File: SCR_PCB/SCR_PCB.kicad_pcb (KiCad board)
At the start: 2 copper layers, 97.4 x 87 mm, 96 parts, among them J2 Conn_01x03, Q1 QM6006D, Q2 QM6006D, Q3 QM6006D, Q4 QM6006D, U2 NA555D, U3 NA555D, U4 SFH617A-1, U5 SFH617A-1, U6 SFH617A-1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

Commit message: Coplete SCR PCB
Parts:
- added G***: LOGO, LOGO, F.Cu at (1.40, -12.0)
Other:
- board text added: "J.Soszyński 17.05.26"
- board text added: "SCR Full Bridge COntroll PCB"

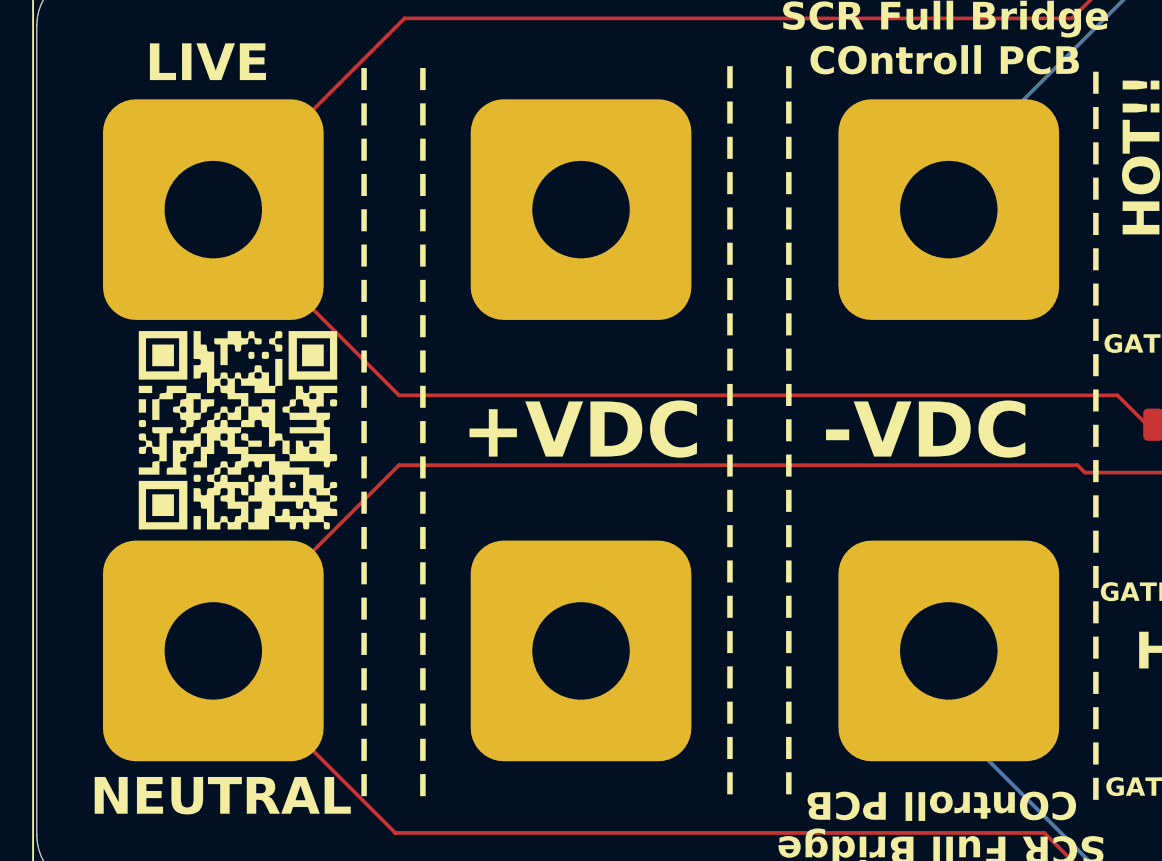
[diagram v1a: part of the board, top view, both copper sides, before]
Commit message: start Controller schematic
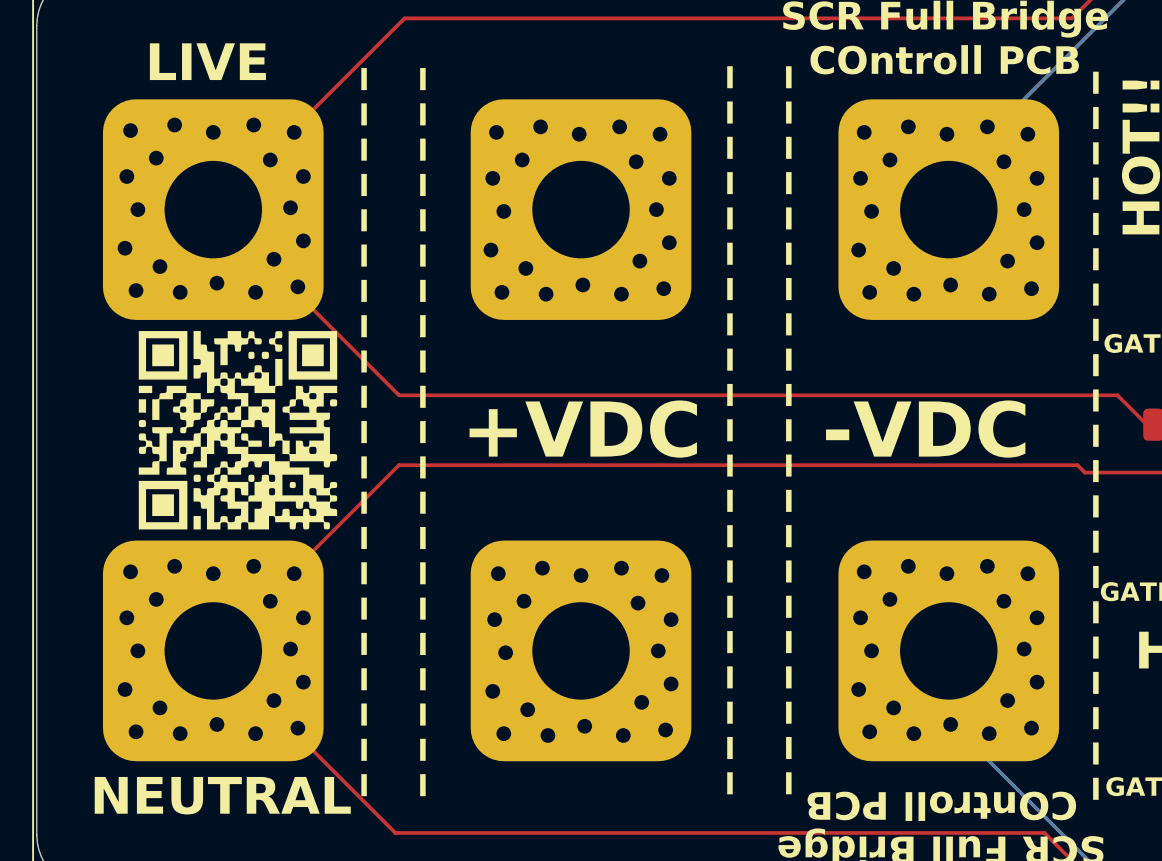
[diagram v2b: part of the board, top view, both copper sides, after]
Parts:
- added ?: , , F.Cu at (0.00, -28.2)
- added ?: , , F.Cu at (-3.10, -26.8)
- added ?: , , F.Cu at (-4.80, 2.10)
- added ?: , , F.Cu at (19.9, -28.1)
- added ?: , , F.Cu at (16.8, -26.7)
- added ?: , , F.Cu at (24.3, -28.1)
- added ?: , , F.Cu at (4.20, -24.1)
- added ?: , , F.Cu at (15.9, 0.10)
- added ?: , , F.Cu at (42.2, 4.50)
- added ?: , , F.Cu at (44.3, -4.20)
- added ?: , , F.Cu at (-2.10, -28.6)
- added ?: , , F.Cu at (18.2, 4.60)
- added ?: , , F.Cu at (20.0, -4.10)
- added ?: , , F.Cu at (3.30, -21.3)
- added ?: , , F.Cu at (38.1, 4.50)
- added ?: , , F.Cu at (17.8, -28.5)
- added ?: , , F.Cu at (3.30, 2.70)
- added ?: , , F.Cu at (35.8, 0.00)
- added ?: , , F.Cu at (-4.10, -24.0)
- added ?: , , F.Cu at (15.8, 4.50)
- added ?: , , F.Cu at (35.7, -19.5)
- added ?: , , F.Cu at (17.1, 3.20)
- added ?: , , F.Cu at (42.1, -28.5)
- added ?: , , F.Cu at (35.2, -25.7)
- added ?: , , F.Cu at (43.0, -26.6)
- added ?: , , F.Cu at (-4.50, -28.3)
- added ?: , , F.Cu at (35.4, -4.30)
- added ?: , , F.Cu at (24.8, -22.2)
- added ?: , , F.Cu at (23.1, -2.60)
- added ?: , , F.Cu at (-3.10, -2.80)
- added ?: , , F.Cu at (-4.70, -25.8)
- added ?: , , F.Cu at (15.7, -19.5)
- added ?: , , F.Cu at (44.1, -0.10)
- added ?: , , F.Cu at (15.2, -25.7)
- added ?: , , F.Cu at (37.8, -4.60)
- added ?: , , F.Cu at (-2.90, 3.10)
- added ?: , , F.Cu at (44.8, -25.7)
- added ?: , , F.Cu at (36.8, -2.80)
- added ?: , , F.Cu at (42.2, -19.4)
- added ?: , , F.Cu at (4.90, -22.3)
- added ?: , , F.Cu at (44.5, -19.7)
- added ?: , , F.Cu at (39.9, -28.1)
- added ?: , , F.Cu at (38.1, -19.4)
- added ?: , , F.Cu at (44.8, -1.80)
- added ?: , , F.Cu at (22.1, -28.5)
- added ?: , , F.Cu at (39.9, -4.20)
- added ?: , , F.Cu at (0.20, 4.00)
- added ?: , , F.Cu at (35.1, -21.8)
- added ?: , , F.Cu at (37.8, -28.5)
- added ?: , , F.Cu at (-4.20, -19.6)
- added ?: , , F.Cu at (15.5, -4.20)
- added ?: , , F.Cu at (24.6, 4.30)
- added ?: , , F.Cu at (17.9, -4.50)
- added ?: , , F.Cu at (44.1, -24.0)
- added ?: , , F.Cu at (35.2, -1.80)
- added ?: , , F.Cu at (4.90, -25.8)
- added ?: , , F.Cu at (22.3, 4.60)
- added ?: , , F.Cu at (-4.80, -21.9)
- added ?: , , F.Cu at (37.0, 3.10)
- added ?: , , F.Cu at (15.2, 2.20)
- added ?: , , F.Cu at (3.10, -26.7)
- added ?: , , F.Cu at (20.2, 4.10)
- added ?: , , F.Cu at (44.3, -28.1)
- added ?: , , F.Cu at (-4.10, 0.00)
- added ?: , , F.Cu at (4.60, -19.8)
- added ?: , , F.Cu at (-4.50, -4.30)
- added ?: , , F.Cu at (24.2, 0.00)
- added ?: , , F.Cu at (42.1, -4.60)
- added ?: , , F.Cu at (0.20, -20.0)
- added ?: , , F.Cu at (35.1, 2.10)
- added ?: , , F.Cu at (24.9, -1.70)
- added ?: , , F.Cu at (2.30, -19.5)
- added ?: , , F.Cu at (37.0, -20.8)
- added ?: , , F.Cu at (2.30, 4.50)
- added ?: , , F.Cu at (16.9, -2.70)
- added ?: , , F.Cu at (44.8, 1.70)
- added ?: , , F.Cu at (35.4, -28.2)
- added ?: , , F.Cu at (24.8, -25.7)
- added ?: , , F.Cu at (-4.70, -1.80)
- added ?: , , F.Cu at (-2.90, -20.9)
- added ?: , , F.Cu at (23.3, 2.80)
- added ?: , , F.Cu at (43.2, 2.70)
- added ?: , , F.Cu at (23.0, -26.6)
- added ?: , , F.Cu at (4.20, -0.10)
- added ?: , , F.Cu at (15.4, -28.2)
- added ?: , , F.Cu at (43.2, -21.2)
- added ?: , , F.Cu at (0.00, -4.20)
- added ?: , , F.Cu at (35.7, 4.40)
- added ?: , , F.Cu at (40.1, 4.00)
- added ?: , , F.Cu at (36.8, -26.7)
- added ?: , , F.Cu at (4.40, -28.2)
- added ?: , , F.Cu at (20.1, -19.9)
- added ?: , , F.Cu at (-1.80, -19.5)
- added ?: , , F.Cu at (4.60, 4.20)
- added ?: , , F.Cu at (24.1, -24.0)
- added ?: , , F.Cu at (15.1, -21.8)
- added ?: , , F.Cu at (44.8, -22.2)
- added ?: , , F.Cu at (-2.10, -4.60)
- added ?: , , F.Cu at (24.9, 1.80)
- added ?: , , F.Cu at (4.90, -1.80)
- added ?: , , F.Cu at (3.10, -2.70)
- added ?: , , F.Cu at (22.2, -19.4)
- added ?: , , F.Cu at (40.1, -19.9)
- added ?: , , F.Cu at (-1.80, 4.50)
- added ?: , , F.Cu at (18.1, -19.4)
- added ?: , , F.Cu at (43.0, -2.70)
- added ?: , , F.Cu at (23.2, -21.2)
- added ?: , , F.Cu at (35.8, -23.9)
- added ?: , , F.Cu at (4.90, 1.70)
- added ?: , , F.Cu at (44.5, 4.20)
- added ?: , , F.Cu at (24.4, -4.10)
- added ?: , , F.Cu at (15.3, -1.70)
- added ?: , , F.Cu at (15.8, -23.9)
- added ?: , , F.Cu at (2.20, -4.60)
- added ?: , , F.Cu at (4.40, -4.20)
- added ?: , , F.Cu at (2.20, -28.6)
- added ?: , , F.Cu at (22.2, -4.50)
- added ?: , , F.Cu at (-4.20, 4.40)
- added ?: , , F.Cu at (17.0, -20.8)
- added ?: , , F.Cu at (24.5, -19.7)
